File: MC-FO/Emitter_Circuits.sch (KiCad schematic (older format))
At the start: 10 parts, among them U21 74ACT08SCX, U22 IFE98

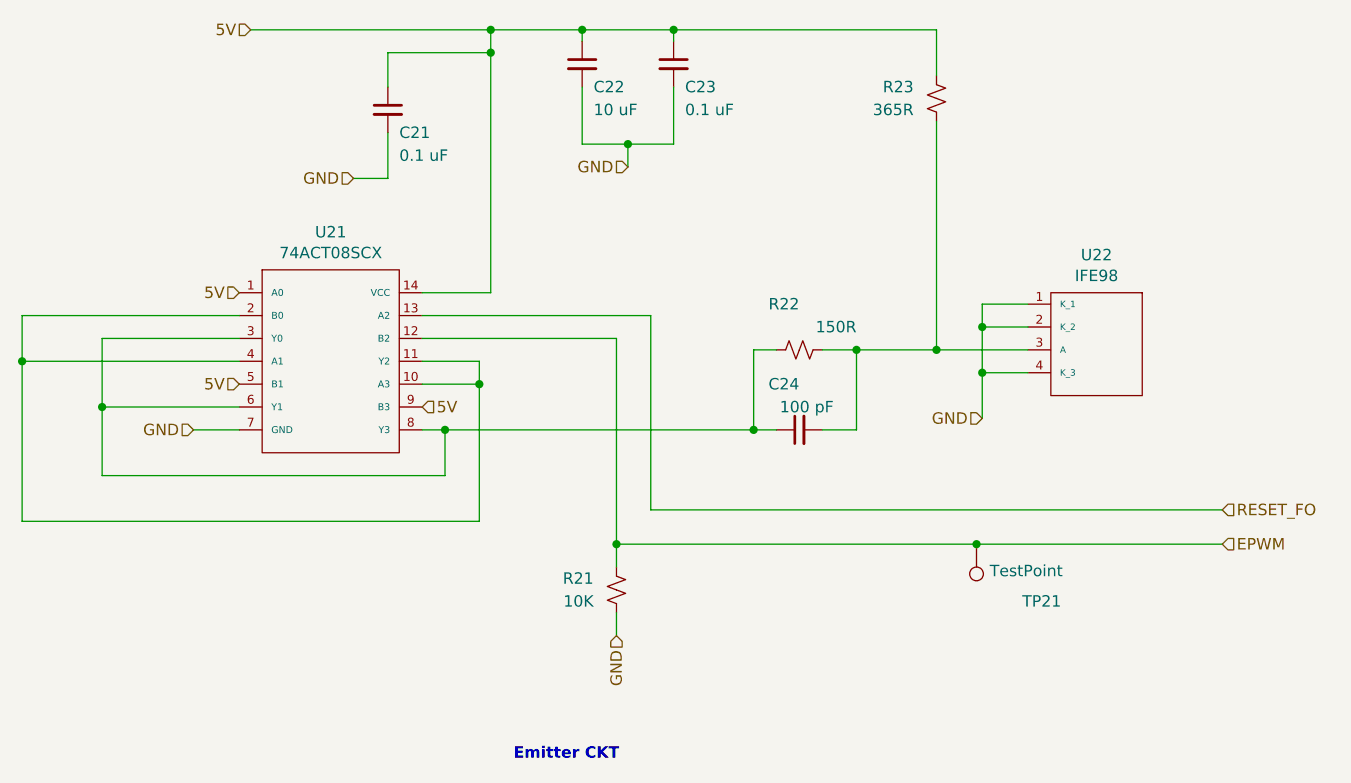
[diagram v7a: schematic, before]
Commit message: Layout Revision
-removed MH1 from emitter/detector symbol
-pin out changes to assist with routing on the backplane
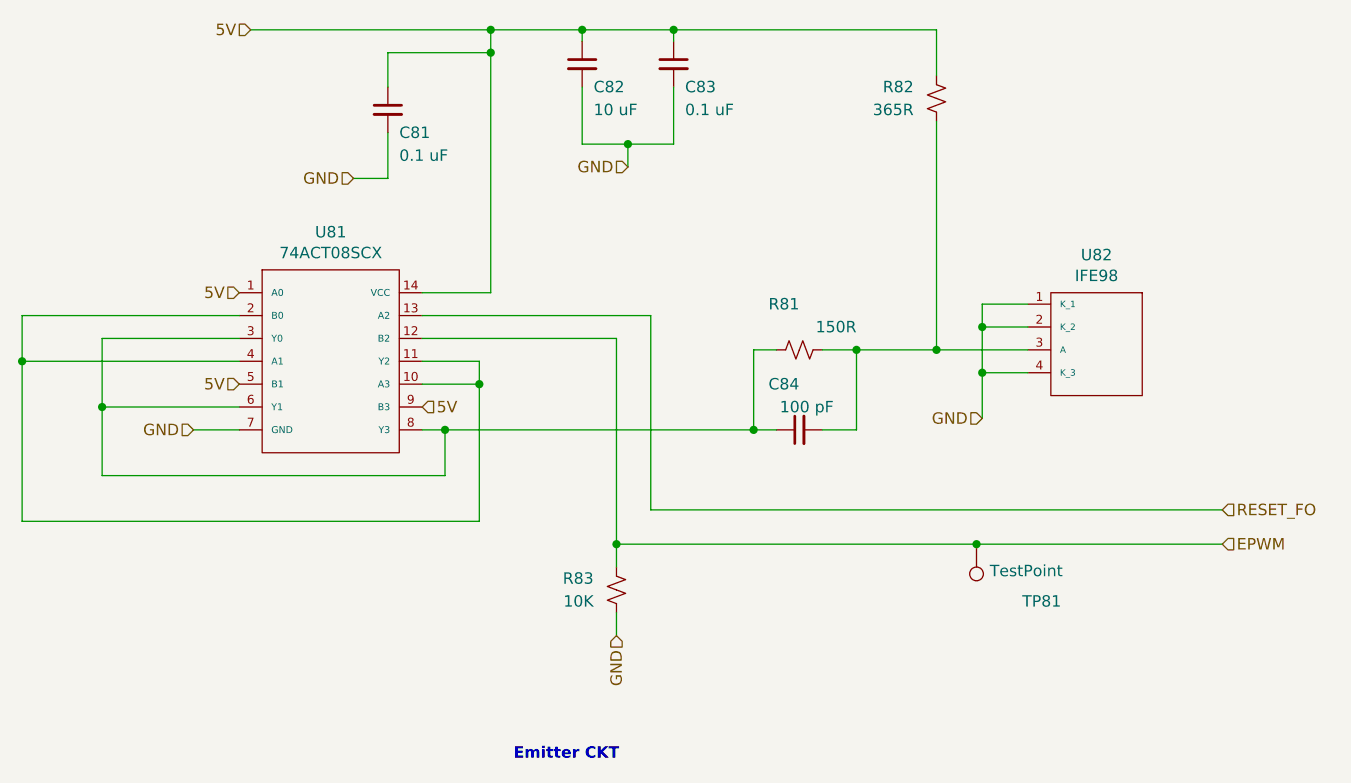
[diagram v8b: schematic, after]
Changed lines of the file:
@@
 $Descr A4 11693 8268
 encoding utf-8
-Sheet 4 11
+Sheet 8 11
 Title ""
 Date ""
@@
 AR Path="/6176CA81/617428A7" Ref="R101"  Part="1"
 AR Path="/6176CAE4/617428A7" Ref="R121"  Part="1"
-F 0 "R22" V 6900 4400 50  0000 L CNN
+F 0 "R81" V 6900 4400 50  0000 L CNN
 F 1 "150R" V 6800 4150 50  0000 L CNN
 F 2 "Resistor_SMD:R_0603_1608Metric" H 6700 4400 50  0001 C CNN
@@
 AR Path="/6176CA81/61748E58" Ref="C104"  Part="1"
 AR Path="/6176CAE4/61748E58" Ref="C124"  Part="1"
-F 0 "C24" V 6900 4750 50  0000 L CNN
+F 0 "C84" V 6900 4750 50  0000 L CNN
 F 1 "100 pF" V 6800 4600 50  0000 L CNN
 F 2 "Capacitor_SMD:C_0603_1608Metric" H 6700 4750 50  0001 C CNN
@@
 AR Path="/6176CA81/6178E7F7" Ref="R102"  Part="1"
 AR Path="/6176CAE4/6178E7F7" Ref="R122"  Part="1"
-F 0 "R23" H 7400 3250 50  0000 L CNN
+F 0 "R82" H 7400 3250 50  0000 L CNN
 F 1 "365R" H 7400 3350 50  0000 L CNN
 F 2 "Resistor_SMD:R_0603_1608Metric" H 7300 3300 50  0001 C CNN
@@
 AR Path="/6176CA81/6171F0C9" Ref="C101"  Part="1"
 AR Path="/6176CAE4/6171F0C9" Ref="C121"  Part="1"
-F 0 "C21" H 4950 3250 50  0000 L CNN
+F 0 "C81" H 4950 3250 50  0000 L CNN
 F 1 "0.1 uF" H 4950 3150 50  0000 L CNN
 F 2 "Capacitor_SMD:C_0603_1608Metric" H 4900 3350 50  0001 C CNN
@@
 AR Path="/6176CA81/61733718" Ref="C103"  Part="1"
 AR Path="/6176CAE4/61733718" Ref="C123"  Part="1"
-F 0 "C23" H 6200 3050 50  0000 L CNN
+F 0 "C83" H 6200 3050 50  0000 L CNN
 F 1 "0.1 uF" H 6200 2950 50  0000 L CNN
 F 2 "Capacitor_SMD:C_0603_1608Metric" H 6150 3150 50  0001 C CNN
@@
 AR Path="/6176CA81/61730A88" Ref="C102"  Part="1"
 AR Path="/6176CAE4/61730A88" Ref="C122"  Part="1"
-F 0 "C22" H 5800 3050 50  0000 L CNN
+F 0 "C82" H 5800 3050 50  0000 L CNN
 F 1 "10 uF" H 5800 2950 50  0000 L CNN
 F 2 "Capacitor_SMD:C_0603_1608Metric" H 5750 3150 50  0001 C CNN
@@
 AR Path="/6176CAE4/61804FDE" Ref="U121"  Part="1"
 AR Path="/61804FDE" Ref="U121"  Part="1"
-F 0 "U21" H 4650 4115 50  0000 C CNN
+F 0 "U81" H 4650 4115 50  0000 C CNN
 F 1 "74ACT08SCX" H 4650 4024 50  0000 C CNN
 F 2 "Package_SO:SOIC-14_3.9x8.7mm_P1.27mm" H 4650 4000 50  0001 C CNN
@@
 AR Path="/6176CAE4/61778B54" Ref="U122"  Part="1"
 AR Path="/617509F7/61778B54" Ref="U42"  Part="1"
-F 0 "U22" H 8000 4215 50  0000 C CNN
+F 0 "U82" H 8000 4215 50  0000 C CNN
 F 1 "IFE98" H 8000 4124 50  0000 C CNN
 F 2 "Footprints_MC-FO:IFE98" H 8000 4100 50  0001 C CNN
@@
 AR Path="/6176CA81/617DC24B" Ref="R103"  Part="1"
 AR Path="/6176CAE4/617DC24B" Ref="R123"  Part="1"
-F 0 "R21" H 6000 5400 50  0000 L CNN
+F 0 "R83" H 6000 5400 50  0000 L CNN
 F 1 "10K" H 6000 5500 50  0000 L CNN
 F 2 "Resistor_SMD:R_0603_1608Metric" H 5900 5450 50  0001 C CNN
@@
 AR Path="/61750A2A/623D825D" Ref="TP61"  Part="1"
 AR Path="/6176CA10/623D825D" Ref="TP81"  Part="1"
-F 0 "TP21" H 7275 5500 50  0000 R CNN
+F 0 "TP81" H 7275 5500 50  0000 R CNN
 F 1 "TestPoint" H 7417 5367 50  0000 R CNN
 F 2 "TestPoint:TestPoint_Pad_D2.0mm" H 7675 5250 50  0001 C CNN
